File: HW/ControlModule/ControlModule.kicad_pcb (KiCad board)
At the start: 2 copper layers, 243.8 x 95.2 mm, 91 parts, among them U1 AD8629, U2 STM32L476VETx, U3 LM4132AMF-3.3, U4 TLV702-Q1

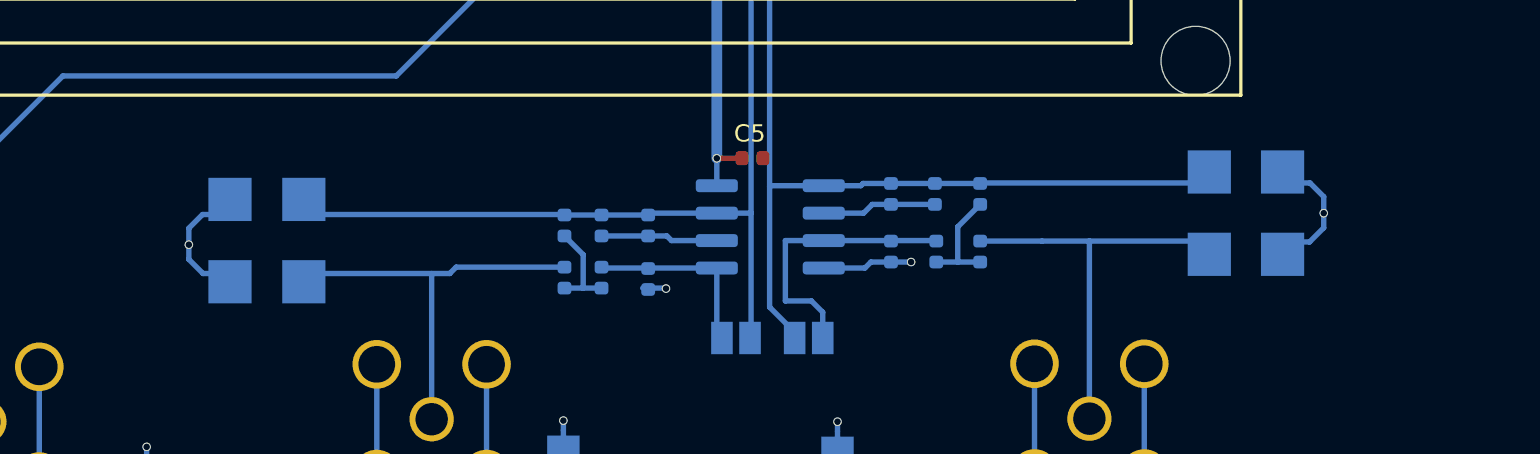
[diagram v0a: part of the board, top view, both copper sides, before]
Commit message: Updates
- New simplified current sink design: see LTSpice model "MOSFET_CurrentSense_NoSignalInversion".
Needs to be confirmed on breadboard!
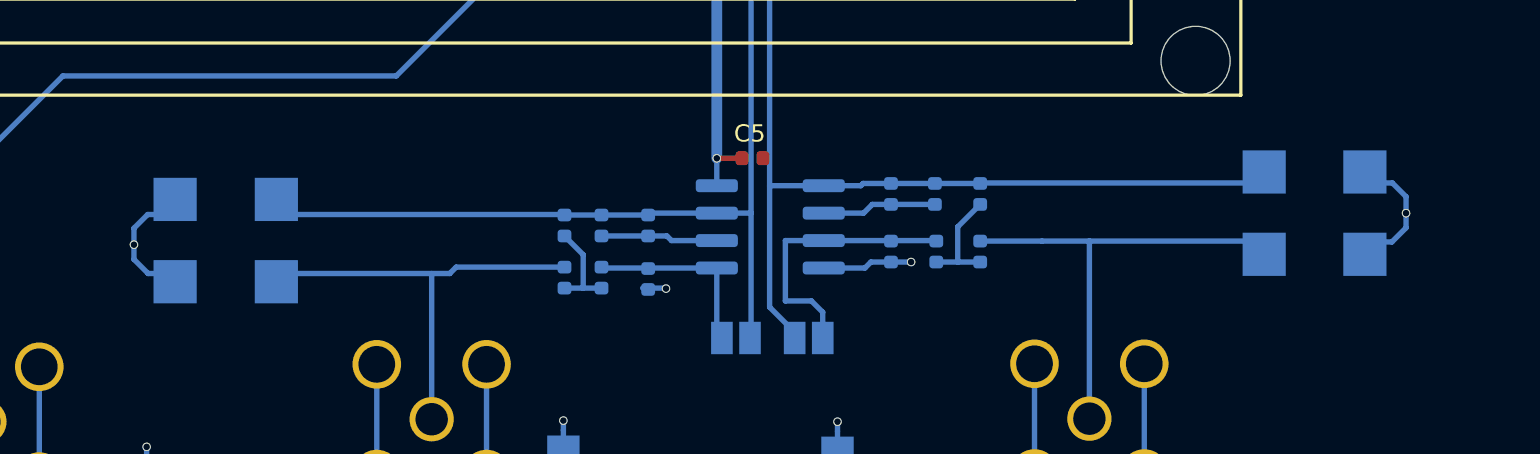
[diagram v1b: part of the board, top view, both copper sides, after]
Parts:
- moved TPG10 3.81 mm to (199.0, 118.7)
- moved TPG9 3.81 mm to (199.0, 122.6)
- moved TPG7 2.54 mm to (143.9, 123.8)
- moved TPG8 2.54 mm to (143.9, 120.0)
- moved TP10 2.54 mm to (194.3, 118.7)
- moved TP2 2.54 mm to (194.3, 122.6)
- moved TP1 1.27 mm to (148.6, 123.8)
- moved TP11 1.27 mm to (148.6, 120.0)
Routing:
- net /Control/ADCSIG1: track 19.3 -> 21.5 mm
- net /Control/ADCS1: track 51.6 -> 53.7 mm
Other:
- board text added: "SWO SWDIO GND SWCLK NRST"
- board text removed: "SWCLK GND SWDIO NRST SWO"

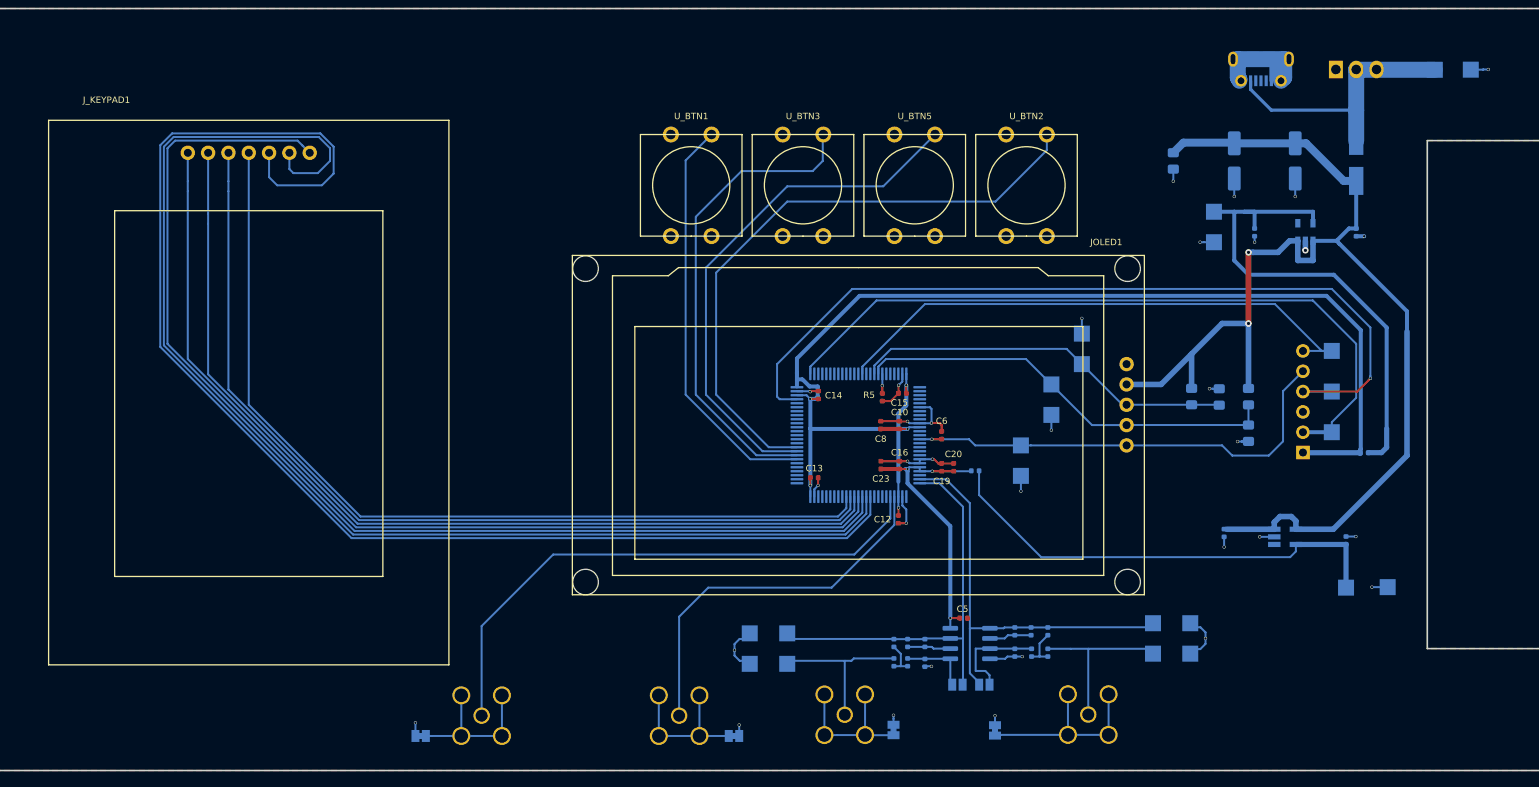
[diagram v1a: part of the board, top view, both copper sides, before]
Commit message: Added Interafec IBOMS
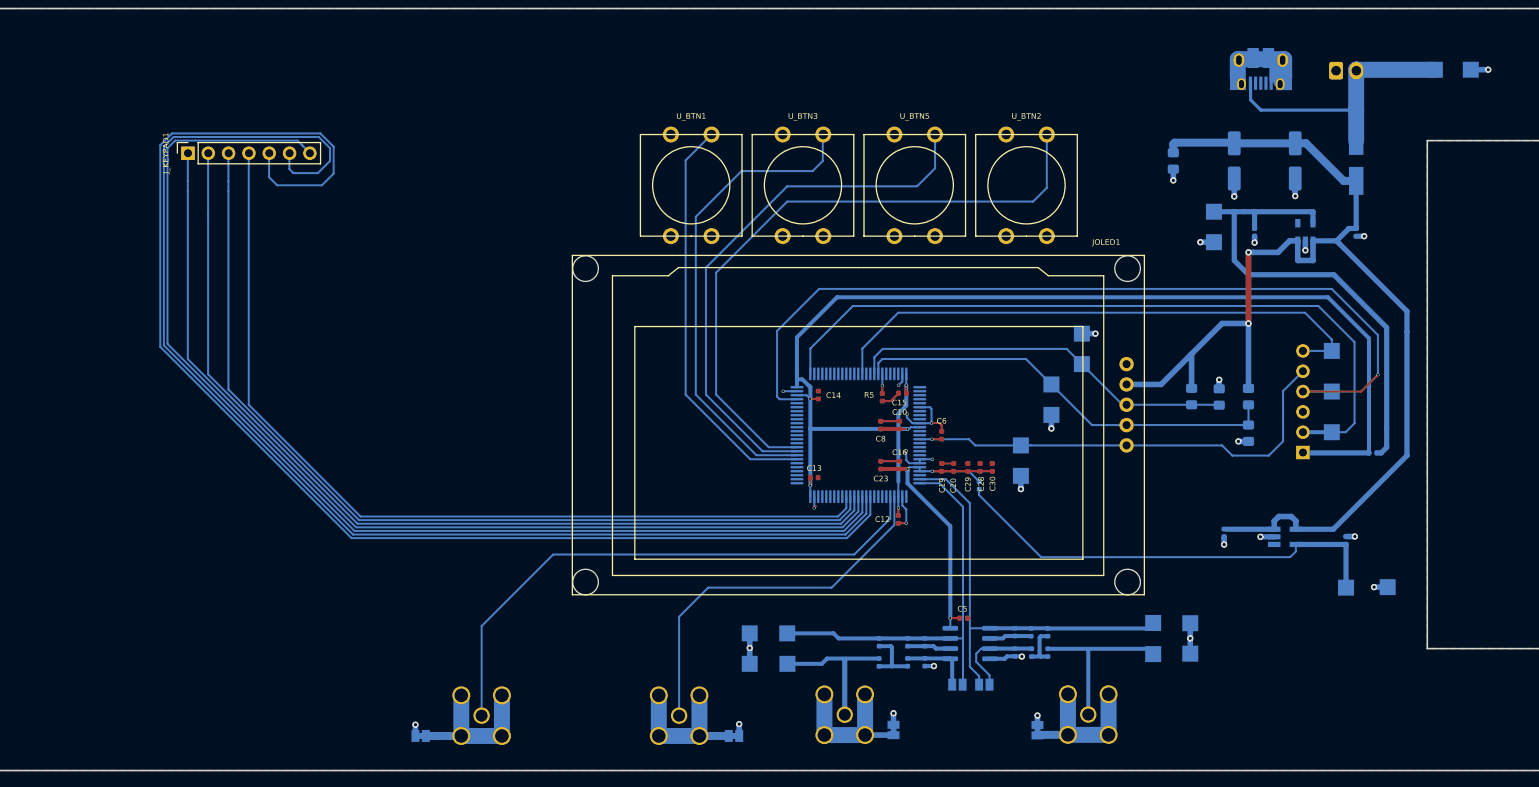
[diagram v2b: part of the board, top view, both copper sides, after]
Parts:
- added C28: 1uF, Capacitor_SMD:C_0402_1005Metric, F.Cu at (172.7, 99.3)
- added C29: 1uF, Capacitor_SMD:C_0402_1005Metric, F.Cu at (171.2, 99.3)
- added C30: 1uF, Capacitor_SMD:C_0402_1005Metric, F.Cu at (174.2, 99.3)
- JPWR1: value KK254_01x03 -> KK254_01x02; footprint Connector_Molex:Molex_KK-254_AE-6410-03A_1x03_P2.54mm_Vertical -> Connector_Molex:Molex_KK-254_AE-6410-02A_1x02_P2.54mm_Vertical
- J_5VUSB1: footprint Connector_USB:USB_Micro-B_Molex-105017-0001 -> Connector_USB:USB_Micro-B_Amphenol_10103594-0001LF_Horizontal
- J_KEYPAD1: value Grayhill-96AB2-102-F -> Samtec ESW elevated PCB socket; footprint Grayhill-96AB2-102-F:Grayhill-96AB2-102-F -> Connector_PinSocket_2.54mm:PinSocket_1x07_P2.54mm_Vertical
- U4: value TLV702-Q1 -> TLV70233DBVR
- moved J_KEYPAD1 31.9 mm to (73.7, 60.0), turned to 90 degrees
- moved JP1 5.31 mm to (179.9, 132.1)
- moved L1 1.90 mm to (172.6, 101.5), turned to 90 degrees
- moved R1 1.85 mm to (160.1, 123.6)
- moved C4 1.83 mm to (160.1, 121.1)
- moved L2 1.07 mm to (221.8, 97.5)
- moved JPWR1 0.15 mm to (217.2, 49.7)
- moved C26 0.13 mm to (179.1, 119.9)
- moved C3 0.13 mm to (181.2, 119.9)
- moved R8 0.10 mm to (177.0, 119.9)
- moved R9 0.09 mm to (163.7, 121.1)
- moved C27 0.09 mm to (165.8, 121.1)
- moved C2 0.08 mm to (165.8, 123.6)
- moved TP2 0.06 mm to (194.3, 122.6)
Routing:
- net GNDS: track 104.4 -> 94.5 mm
- net +3.3VA: track 38.2 -> 44.2 mm
- net Net-(JADC1-Pad2): track 24.3 -> 19.1 mm
- net /Control/SWDIO: track 105.8 -> 109.3 mm
- net Net-(C4-Pad2): track 4.49 -> 7.61 mm
- net /Control/BTN4: track 77.7 -> 80.5 mm
- net /Control/BTN3: track 65.7 -> 68.2 mm
- net Net-(C21-Pad2): track 58.6 -> 56.3 mm
- net /Control/SWCLK: track 90.7 -> 92.3 mm
- net /Control/ADCSIG2: track 20.0 -> 18.7 mm
- net /Control/SWO: track 68.9 -> 70.2 mm
- net Net-(C1-Pad1): track 12.9 -> 11.8 mm
- net +3V3: track 159.3 -> 160.5 mm
- net Net-(C22-Pad1): track 63.3 -> 62.3 mm
- net /Control/ADCS2: track 50.7 -> 51.7 mm
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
